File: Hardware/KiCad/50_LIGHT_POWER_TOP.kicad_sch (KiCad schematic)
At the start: 0 parts

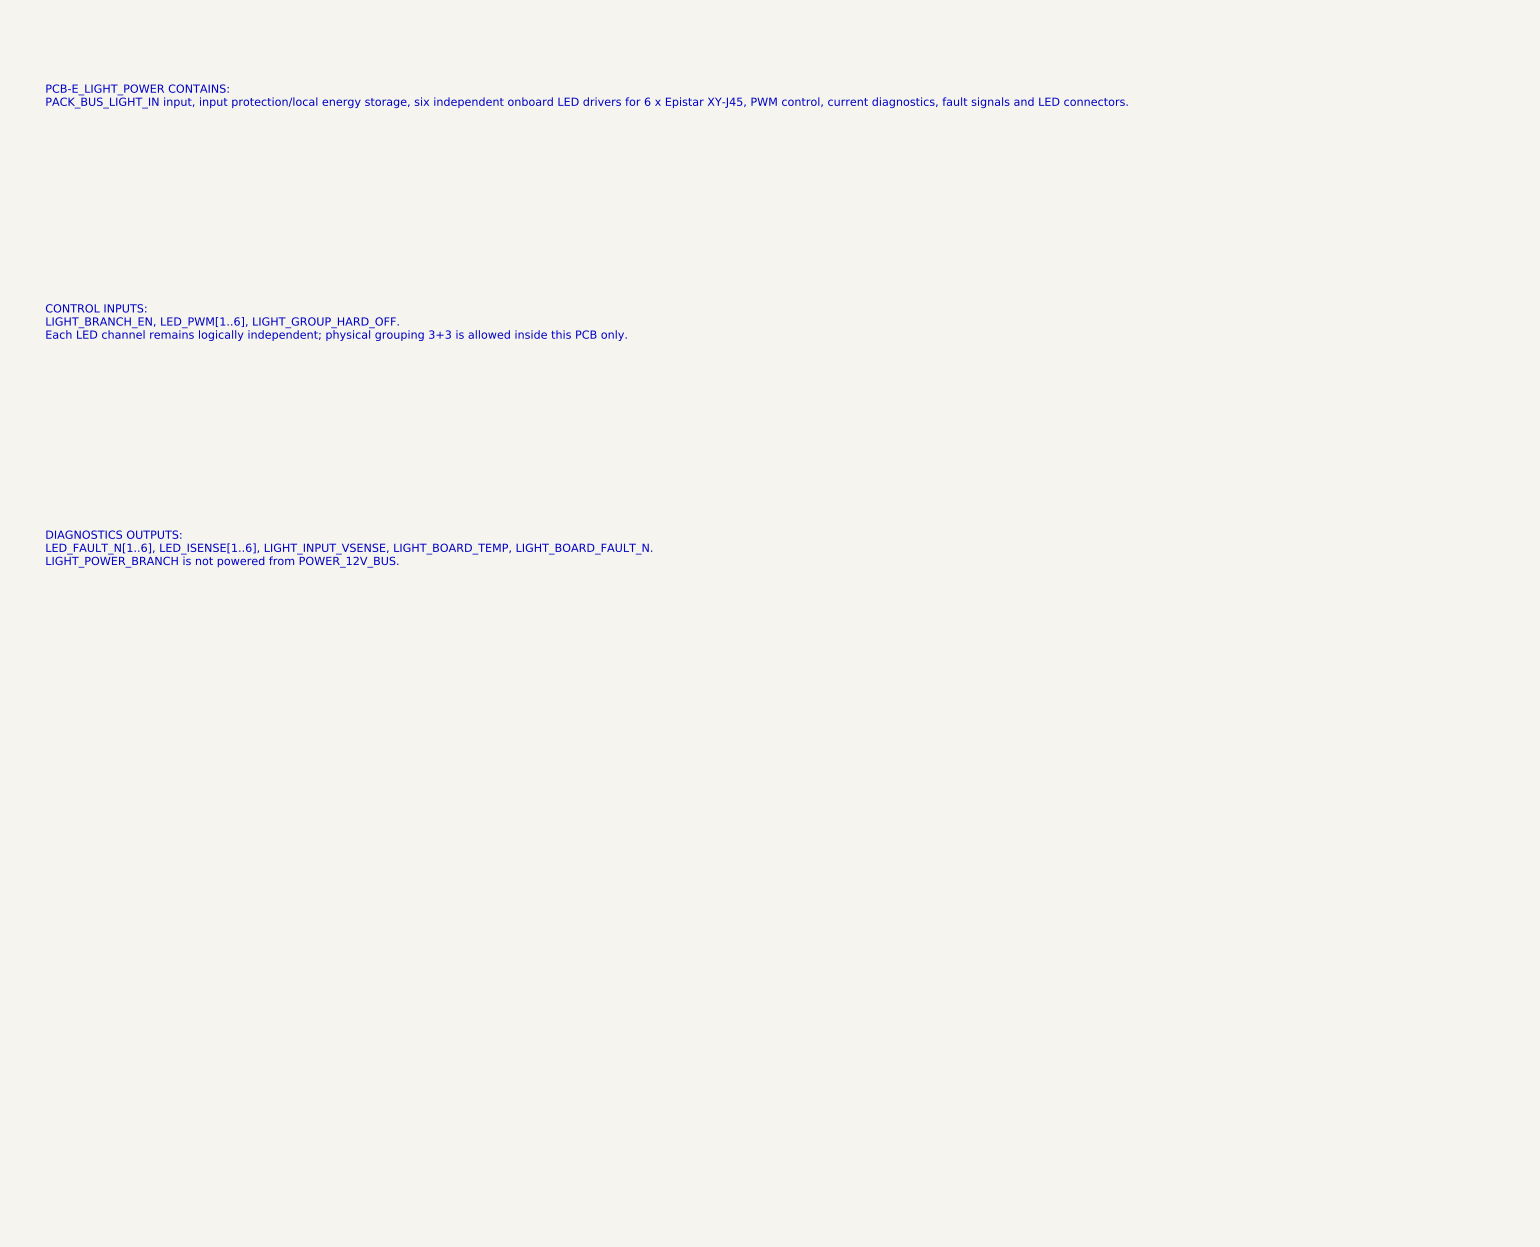
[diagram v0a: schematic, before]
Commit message: hardware: detail 50 light power top sheet
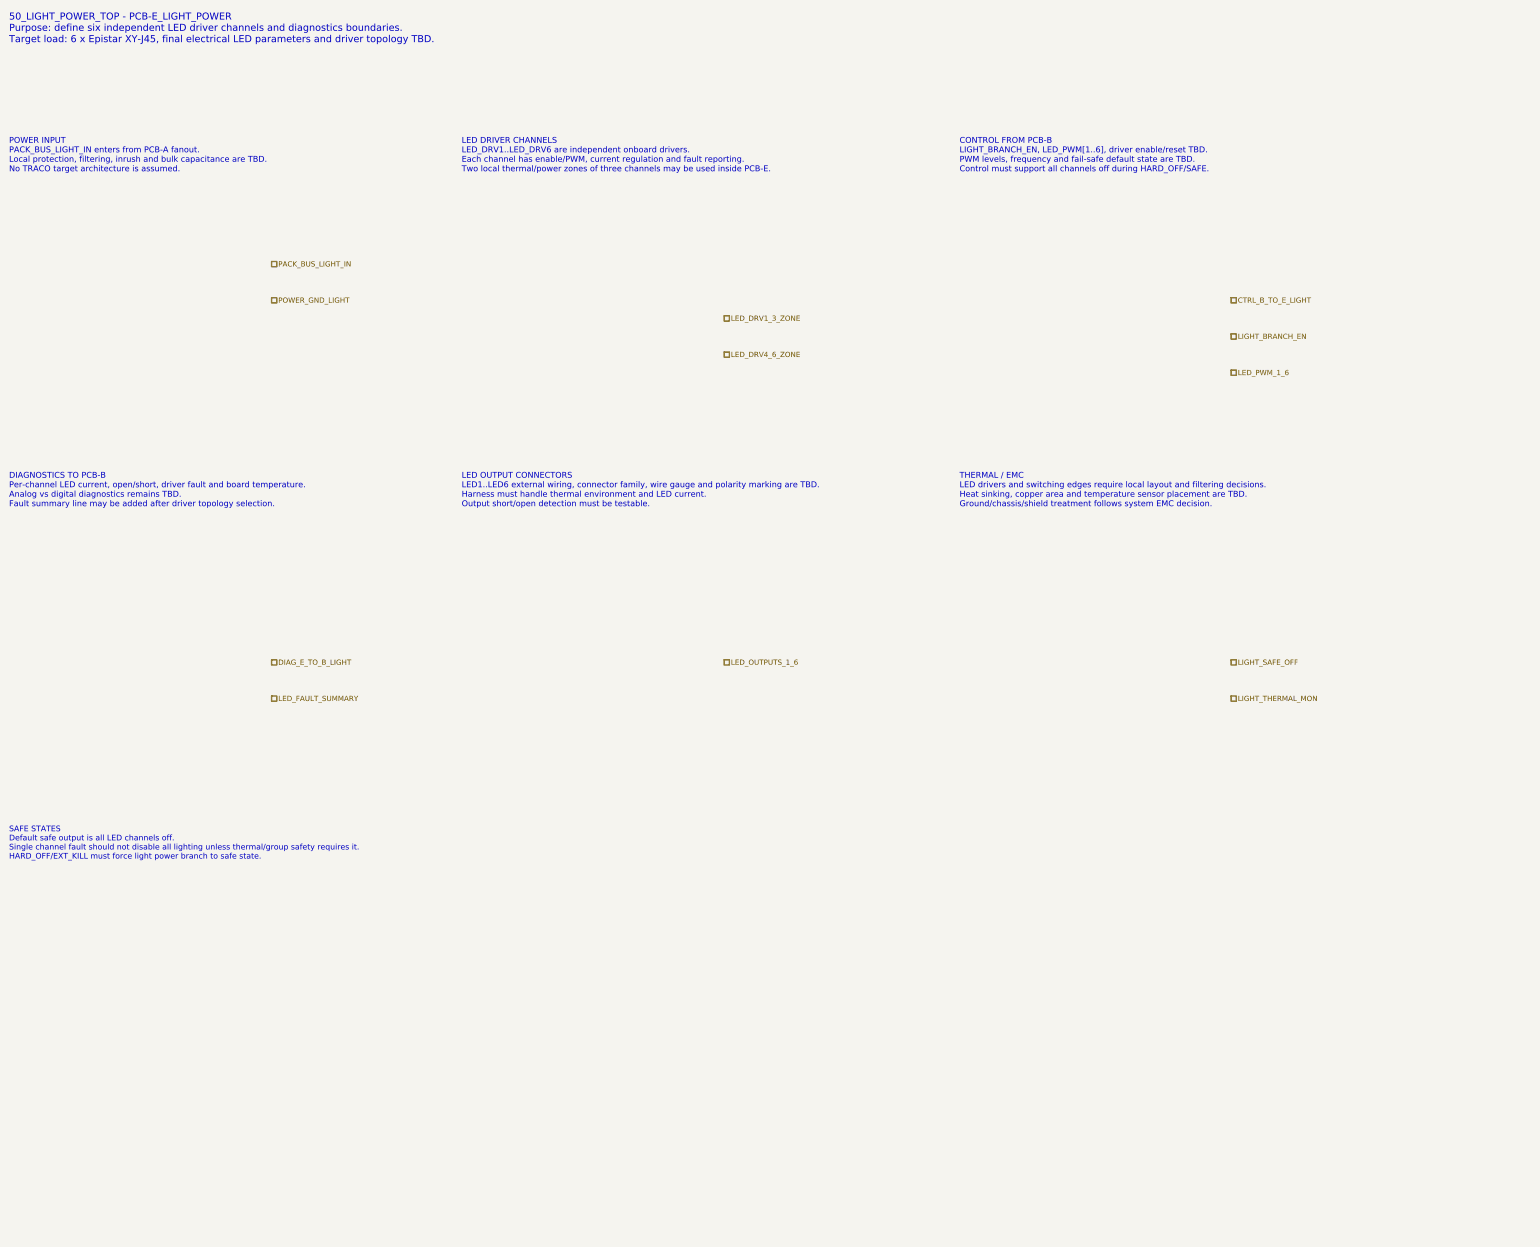
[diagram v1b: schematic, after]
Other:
- note added: "50_LIGHT_POWER_TOP - PCB-E_LIGHT_POWER Purpose: define six independent LED driver channels and diagnostics boundaries. Target load: 6 x Epistar XY-J45, final electrical LED parameters and driver topology TBD."
- note added: "CONTROL FROM PCB-B LIGHT_BRANCH_EN, LED_PWM[1..6], driver enable/reset TBD. PWM levels, frequency and fail-safe default state are TBD. Control must support all channels off during HARD_OFF/SAFE."
- note added: "DIAGNOSTICS TO PCB-B Per-channel LED current, open/short, driver fault and board temperature. Analog vs digital diagnostics remains TBD. Fault summary line may be added after driver topology selection."
- note added: "LED DRIVER CHANNELS LED_DRV1..LED_DRV6 are independent onboard drivers. Each channel has enable/PWM, current regulation and fault reporting. Two local thermal/power zones of three channels may be used inside PCB-E."
- note added: "LED OUTPUT CONNECTORS LED1..LED6 external wiring, connector family, wire gauge and polarity marking are TBD. Harness must handle thermal environment and LED current. Output short/open detection must be testable."
- note added: "POWER INPUT PACK_BUS_LIGHT_IN enters from PCB-A fanout. Local protection, filtering, inrush and bulk capacitance are TBD. No TRACO target architecture is assumed."
- note added: "SAFE STATES Default safe output is all LED channels off. Single channel fault should not disable all lighting unless thermal/group safety requires it. HARD_OFF/EXT_KILL must force light power branch to safe state."
- note added: "THERMAL / EMC LED drivers and switching edges require local layout and filtering decisions. Heat sinking, copper area and temperature sensor placement are TBD. Ground/chassis/shield treatment follows system EMC decision."
- note removed: "CONTROL INPUTS: LIGHT_BRANCH_EN, LED_PWM[1..6], LIGHT_GROUP_HARD_OFF. Each LED channel remains logically independent; physical grouping 3+3 is allowed inside this PCB only."
- note removed: "DIAGNOSTICS OUTPUTS: LED_FAULT_N[1..6], LED_ISENSE[1..6], LIGHT_INPUT_VSENSE, LIGHT_BOARD_TEMP, LIGHT_BOARD_FAULT_N. LIGHT_POWER_BRANCH is not powered from POWER_12V_BUS."
- note removed: "PCB-E_LIGHT_POWER CONTAINS: PACK_BUS_LIGHT_IN input, input protection/local energy storage, six independent onboard LED drivers for 6 x Epistar XY-J45, PWM control, current diagnostics, fault signals and LED connectors."
- company: (none) -> Gonoboben/plataVM
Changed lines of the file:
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@@
 	(title_block
 		(title "50_LIGHT_POWER_TOP - PCB-E_LIGHT_POWER")
-		(date "2026-07-14")
-		(rev "A0")
-		(comment 1 "Six independent LED driver channels")
+		(date "2026-07-15")
+		(rev "A1")
+		(company "Gonoboben/plataVM")
+		(comment 1 "Architecture Level A: six independent LED driver channels")
+		(comment 2 "No LED driver part numbers or footprints selected")
 	)
-	(text "PCB-E_LIGHT_POWER CONTAINS:\nPACK_BUS_LIGHT_IN input, input protection/local energy storage, six independent onboard LED drivers for 6 x Epistar XY-J45, PWM control, current diagnostics, fault signals and LED connectors."
+	(text "50_LIGHT_POWER_TOP - PCB-E_LIGHT_POWER\nPurpose: define six independent LED driver channels and diagnostics boundaries.\nTarget load: 6 x Epistar XY-J45, final electrical LED parameters and driver topology TBD."
 		(exclude_from_sim no)
-		(at 20 25 0)
-		(effects
-			(font
-				(size 1.8 1.8)
-			)
-			(justify left)
-		)
+		(at 12 10 0)
+		(effects (font (size 1.55 1.55)) (justify left))
+		(uuid "light-text-0001")
 	)
-	(text "CONTROL INPUTS:\nLIGHT_BRANCH_EN, LED_PWM[1..6], LIGHT_GROUP_HARD_OFF.\nEach LED channel remains logically independent; physical grouping 3+3 is allowed inside this PCB only."
+	(text "POWER INPUT\nPACK_BUS_LIGHT_IN enters from PCB-A fanout.\nLocal protection, filtering, inrush and bulk capacitance are TBD.\nNo TRACO target architecture is assumed."
 		(exclude_from_sim no)
-		(at 20 75 0)
-		(effects
-			(font
-				(size 1.8 1.8)
-			)
-			(justify left)
-		)
+		(at 12 38 0)
+		(effects (font (size 1.3 1.3)) (justify left))
+		(uuid "light-text-0002")
 	)
-	(text "DIAGNOSTICS OUTPUTS:\nLED_FAULT_N[1..6], LED_ISENSE[1..6], LIGHT_INPUT_VSENSE, LIGHT_BOARD_TEMP, LIGHT_BOARD_FAULT_N.\nLIGHT_POWER_BRANCH is not powered from POWER_12V_BUS."
+	(text "LED DRIVER CHANNELS\nLED_DRV1..LED_DRV6 are independent onboard drivers.\nEach channel has enable/PWM, current regulation and fault reporting.\nTwo local thermal/power zones of three channels may be used inside PCB-E."
 		(exclude_from_sim no)
-		(at 20 125 0)
-		(effects
-			(font
-				(size 1.8 1.8)
-			)
-			(justify left)
-		)
+		(at 112 38 0)
+		(effects (font (size 1.3 1.3)) (justify left))
+		(uuid "light-text-0003")
 	)
+	(text "CONTROL FROM PCB-B\nLIGHT_BRANCH_EN, LED_PWM[1..6], driver enable/reset TBD.\nPWM levels, frequency and fail-safe default state are TBD.\nControl must support all channels off during HARD_OFF/SAFE."
+		(exclude_from_sim no)
+		(at 222 38 0)
+		(effects (font (size 1.3 1.3)) (justify left))
+		(uuid "light-text-0004")
+	)
+	(text "DIAGNOSTICS TO PCB-B\nPer-channel LED current, open/short, driver fault and board temperature.\nAnalog vs digital diagnostics remains TBD.\nFault summary line may be added after driver topology selection."
+		(exclude_from_sim no)
+		(at 12 112 0)
+		(effects (font (size 1.3 1.3)) (justify left))
+		(uuid "light-text-0005")
+	)
+	(text "LED OUTPUT CONNECTORS\nLED1..LED6 external wiring, connector family, wire gauge and polarity marking are TBD.\nHarness must handle thermal environment and LED current.\nOutput short/open detection must be testable."
+		(exclude_from_sim no)
+		(at 112 112 0)
+		(effects (font (size 1.3 1.3)) (justify left))
+		(uuid "light-text-0006")
+	)
+	(text "THERMAL / EMC\nLED drivers and switching edges require local layout and filtering decisions.\nHeat sinking, copper area and temperature sensor placement are TBD.\nGround/chassis/shield treatment follows system EMC decision."
+		(exclude_from_sim no)
+		(at 222 112 0)
+		(effects (font (size 1.3 1.3)) (justify left))
+		(uuid "light-text-0007")
+	)
+	(text "SAFE STATES\nDefault safe output is all LED channels off.\nSingle channel fault should not disable all lighting unless thermal/group safety requires it.\nHARD_OFF/EXT_KILL must force light power branch to safe state."
+		(exclude_from_sim no)
+		(at 12 190 0)
+		(effects (font (size 1.25 1.25)) (justify left))
+		(uuid "light-text-0008")
+	)
+	(hierarchical_label "PACK_BUS_LIGHT_IN" (shape passive) (exclude_from_sim no) (at 70 62 0) (effects (font (size 1.15 1.15)) (justify left)) (uuid "light-label-0001"))
+	(hierarchical_label "POWER_GND_LIGHT" (shape passive) (exclude_from_sim no) (at 70 70 0) (effects (font (size 1.15 1.15)) (justify left)) (uuid "light-label-0002"))
+	(hierarchical_label "CTRL_B_TO_E_LIGHT" (shape passive) (exclude_from_sim no) (at 282 70 0) (effects (font (size 1.15 1.15)) (justify left)) (uuid "light-label-0003"))
+	(hierarchical_label "LIGHT_BRANCH_EN" (shape passive) (exclude_from_sim no) (at 282 78 0) (effects (font (size 1.15 1.15)) (justify left)) (uuid "light-label-0004"))
+	(hierarchical_label "LED_PWM_1_6" (shape passive) (exclude_from_sim no) (at 282 86 0) (effects (font (size 1.15 1.15)) (justify left)) (uuid "light-label-0005"))
+	(hierarchical_label "LED_DRV1_3_ZONE" (shape passive) (exclude_from_sim no) (at 170 74 0) (effects (font (size 1.15 1.15)) (justify left)) (uuid "light-label-0006"))
+	(hierarchical_label "LED_DRV4_6_ZONE" (shape passive) (exclude_from_sim no) (at 170 82 0) (effects (font (size 1.15 1.15)) (justify left)) (uuid "light-label-0007"))
+	(hierarchical_label "DIAG_E_TO_B_LIGHT" (shape passive) (exclude_from_sim no) (at 70 150 0) (effects (font (size 1.15 1.15)) (justify left)) (uuid "light-label-0008"))
+	(hierarchical_label "LED_FAULT_SUMMARY" (shape passive) (exclude_from_sim no) (at 70 158 0) (effects (font (size 1.15 1.15)) (justify left)) (uuid "light-label-0009"))
+	(hierarchical_label "LED_OUTPUTS_1_6" (shape passive) (exclude_from_sim no) (at 170 150 0) (effects (font (size 1.15 1.15)) (justify left)) (uuid "light-label-0010"))
+	(hierarchical_label "LIGHT_SAFE_OFF" (shape passive) (exclude_from_sim no) (at 282 150 0) (effects (font (size 1.15 1.15)) (justify left)) (uuid "light-label-0011"))
+	(hierarchical_label "LIGHT_THERMAL_MON" (shape passive) (exclude_from_sim no) (at 282 158 0) (effects (font (size 1.15 1.15)) (justify left)) (uuid "light-label-0012"))
 )
